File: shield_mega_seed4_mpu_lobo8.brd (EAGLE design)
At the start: 99.3 x 72.4 mm, 32 parts, among them U1 GY-521MPU6050

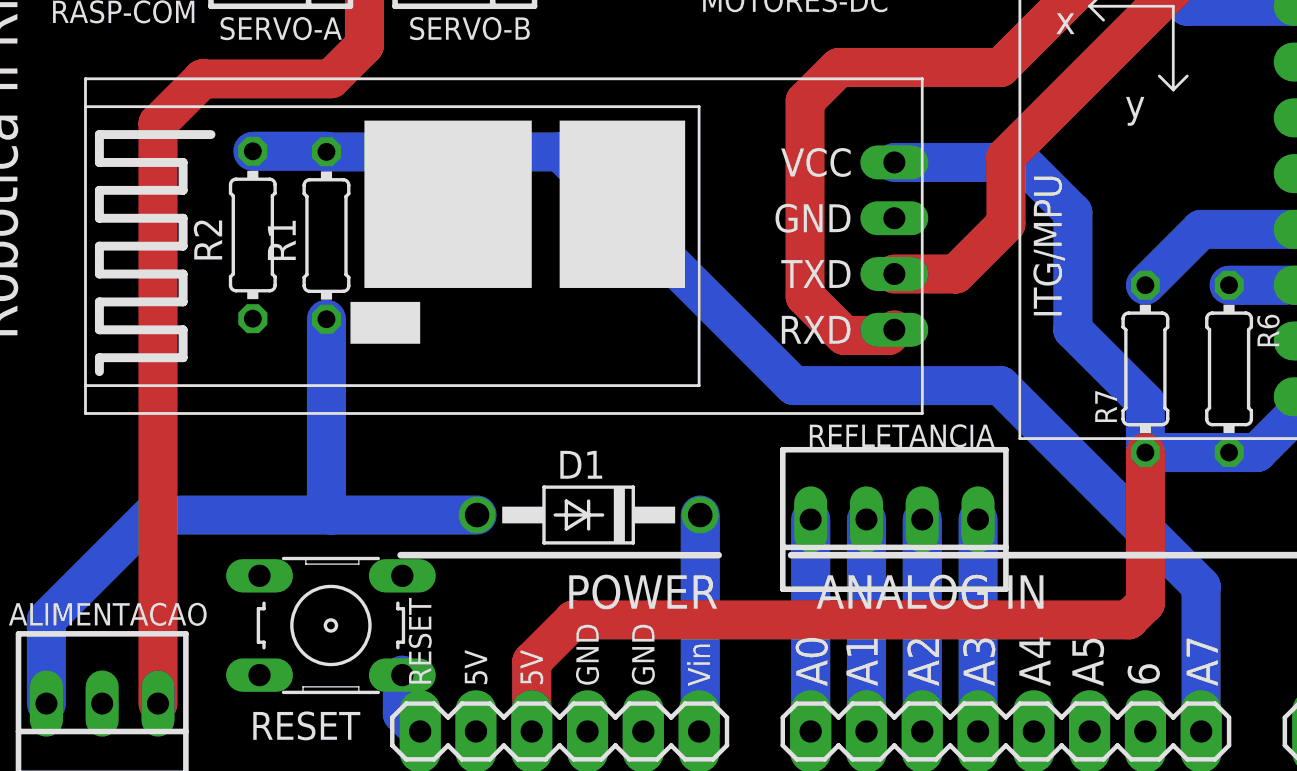
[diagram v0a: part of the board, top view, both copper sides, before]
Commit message: modificação da posição das resistências do divisor de tensão
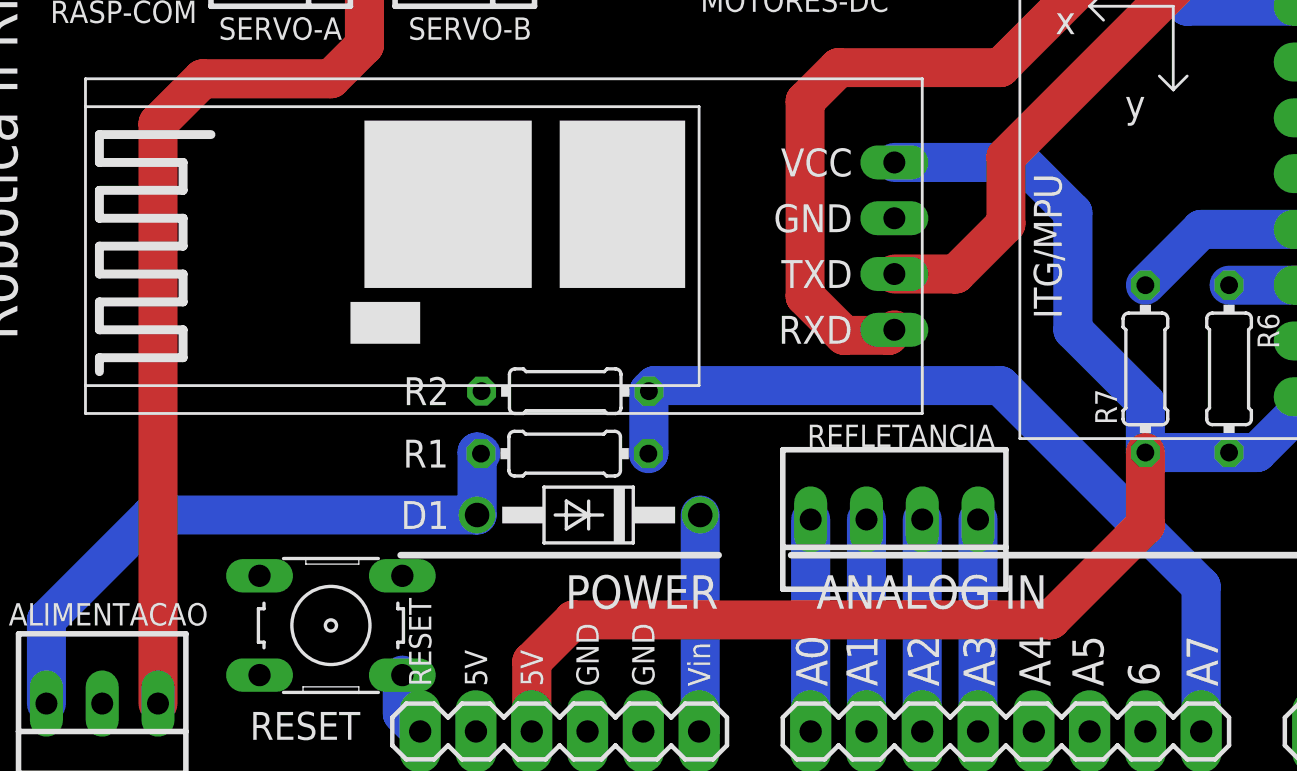
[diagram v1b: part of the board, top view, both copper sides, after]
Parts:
- moved R2 15.9 mm to (28.2, 35.8), turned to 0 degrees
- moved R1 14.7 mm to (28.2, 33.0), turned to 0 degrees
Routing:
- net N$20: track 58.0 -> 38.5 mm
- net VIN: track 34.4 -> 28.5 mm
- net +5V/1: track 69.1 -> 67.0 mm
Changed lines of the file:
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@@
 <attribute name="VALUE" x="76.2" y="26.67" size="1.016" layer="27" ratio="10" rot="R90"/>
 </element>
-<element name="R1" library="rcl" package="0204/7" value="82K" x="17.3228" y="42.9006" smashed="yes" rot="R90">
-<attribute name="NAME" x="15.9258" y="41.6306" size="1.27" layer="25" ratio="10" rot="R90"/>
-<attribute name="VALUE" x="18.0086" y="41.2496" size="1.27" layer="27" ratio="10" rot="R90"/>
-</element>
-<element name="R2" library="rcl" package="0204/7" value="100k" x="13.97" y="42.926" smashed="yes" rot="R90">
-<attribute name="NAME" x="12.573" y="41.656" size="1.27" layer="25" ratio="10" rot="R90"/>
-<attribute name="VALUE" x="14.6558" y="40.64" size="1.27" layer="27" ratio="10" rot="R90"/>
+<element name="R1" library="rcl" package="0204/7" value="82K" x="28.1686" y="32.9692" smashed="yes">
+<attribute name="NAME" x="20.8026" y="32.3342" size="1.27" layer="25" ratio="10"/>
+<attribute name="VALUE" x="26.5176" y="32.2834" size="1.27" layer="27" ratio="10"/>
+</element>
+<element name="R2" library="rcl" package="0204/7" value="100k" x="28.194" y="35.814" smashed="yes">
+<attribute name="NAME" x="20.828" y="35.179" size="1.27" layer="25" ratio="10"/>
+<attribute name="VALUE" x="25.908" y="35.1282" size="1.27" layer="27" ratio="10"/>
 </element>
 <element name="R3" library="rcl" package="0207/7" value="220" x="86.36" y="19.685" smashed="yes">
@@
 <element name="R7" library="rcl" package="0204/7" value="10k" x="54.61" y="36.83" rot="R90"/>
 <element name="D1" library="diode" package="DO41-10" value="" x="29.2608" y="30.1752" smashed="yes" rot="R180">
-<attribute name="NAME" x="30.0228" y="33.0962" size="1.27" layer="25" ratio="10" rot="R180"/>
+<attribute name="NAME" x="22.9108" y="30.8102" size="1.27" layer="25" ratio="10" rot="R180"/>
 <attribute name="VALUE" x="31.2928" y="32.9692" size="1.27" layer="27" ratio="10" rot="R180"/>
 </element>
@@
 <contactref element="D1" pad="A"/>
 <contactref element="ALIMENTACAO" pad="3"/>
-<wire x1="24.1808" y1="30.1752" x2="17.526" y2="30.1752" width="1.778" layer="16"/>
-<wire x1="17.526" y1="30.1752" x2="9.3472" y2="30.1752" width="1.778" layer="16"/>
-<wire x1="17.3228" y1="39.0906" x2="17.3228" y2="30.3784" width="1.778" layer="16"/>
-<wire x1="17.3228" y1="30.3784" x2="17.526" y2="30.1752" width="1.778" layer="16"/>
+<wire x1="24.1808" y1="30.1752" x2="9.3472" y2="30.1752" width="1.778" layer="16"/>
 <wire x1="9.3472" y1="30.1752" x2="4.572" y2="25.4" width="1.778" layer="16"/>
 <wire x1="4.572" y1="25.4" x2="4.572" y2="21.59" width="1.778" layer="16"/>
+<wire x1="24.1808" y1="30.1752" x2="24.1808" y2="33.0454" width="1.778" layer="16"/>
+<wire x1="24.1808" y1="33.0454" x2="24.3586" y2="32.9692" width="1.778" layer="16"/>
 </signal>
 <signal name="VDD">
@@
 <contactref element="B1" pad="A7"/>
 <wire x1="57.15" y1="26.924" x2="57.15" y2="20.32" width="1.778" layer="16"/>
-<wire x1="13.97" y1="46.736" x2="17.2974" y2="46.736" width="1.778" layer="16"/>
-<wire x1="17.2974" y1="46.736" x2="17.3228" y2="46.7106" width="1.778" layer="16"/>
-<wire x1="17.3228" y1="46.7106" x2="27.9654" y2="46.7106" width="1.778" layer="16"/>
-<wire x1="27.9654" y1="46.7106" x2="38.608" y2="36.068" width="1.778" layer="16"/>
-<wire x1="38.608" y1="36.068" x2="48.006" y2="36.068" width="1.778" layer="16"/>
+<wire x1="32.258" y1="36.068" x2="48.006" y2="36.068" width="1.778" layer="16"/>
 <wire x1="48.006" y1="36.068" x2="57.15" y2="26.924" width="1.778" layer="16"/>
+<wire x1="32.258" y1="36.068" x2="32.004" y2="35.814" width="1.778" layer="16"/>
+<wire x1="32.004" y1="35.814" x2="32.004" y2="32.9946" width="1.778" layer="16"/>
+<wire x1="32.004" y1="32.9946" x2="31.9786" y2="32.9692" width="1.778" layer="16"/>
 </signal>
 <signal name="5V">
@@
 <wire x1="51.308" y1="43.942" x2="49.022" y2="46.228" width="1.778" layer="16"/>
 <wire x1="49.022" y1="46.228" x2="43.18" y2="46.228" width="1.778" layer="16"/>
-<wire x1="54.61" y1="26.162" x2="54.61" y2="33.02" width="1.778" layer="1"/>
-<wire x1="28.575" y1="25.4" x2="53.848" y2="25.4" width="1.778" layer="1"/>
-<wire x1="53.848" y1="25.4" x2="54.61" y2="26.162" width="1.778" layer="1"/>
+<wire x1="28.575" y1="25.4" x2="50.292" y2="25.4" width="1.778" layer="1"/>
+<wire x1="50.292" y1="25.4" x2="54.61" y2="29.718" width="1.778" layer="1"/>
+<wire x1="54.61" y1="29.718" x2="54.61" y2="33.02" width="1.778" layer="1"/>
 </signal>
 <signal name="N$14">
